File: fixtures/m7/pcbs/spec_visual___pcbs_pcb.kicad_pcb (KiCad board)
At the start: 2 copper layers, 1 part

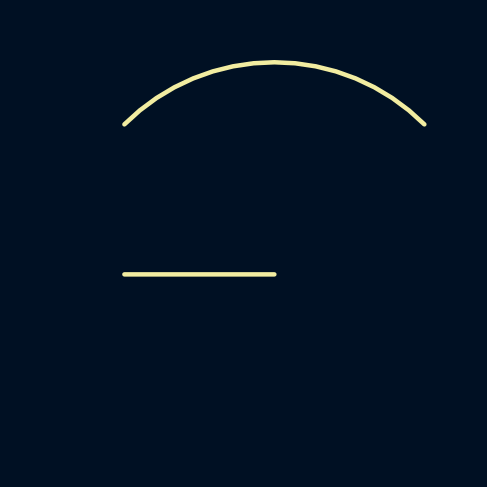
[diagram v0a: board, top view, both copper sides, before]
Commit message: Expand footprint specs and add JS footprints plan
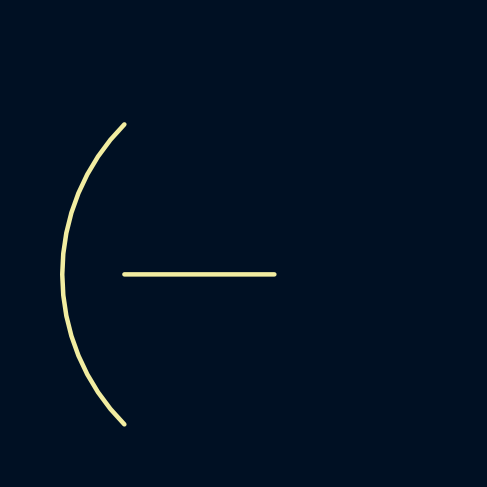
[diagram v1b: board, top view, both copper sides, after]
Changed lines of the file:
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@@
             (fp_text reference "FP1" (at 0 0) (layer F.SilkS) hide (effects (font (size 1.27 1.27) (thickness 0.15))))
             (fp_text value "" (at 0 0) (layer F.SilkS) hide (effects (font (size 1.27 1.27) (thickness 0.15))))
-            (fp_arc (start 5 0) (end 0 -5) (angle 90) (layer F.SilkS) (width 0.15))
+            (fp_arc (start 5 0) (end 0 5) (angle 90) (layer F.SilkS) (width 0.15))
             (fp_line (start 0 0) (end 5 0) (layer F.SilkS) (width 0.15))
-            (fp_text user "ARC90" (at 0 -7 30) (layer F.SilkS) hide (effects (font (size 1.2 1.2) (thickness 0.15)) (justify right)))
+            (fp_text user "ARC90" (at 0 7 30) (layer F.SilkS) hide (effects (font (size 1.2 1.2) (thickness 0.15)) (justify right)))
         )
 )
